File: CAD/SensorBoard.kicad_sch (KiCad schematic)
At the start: 82 parts, among them J1 USB C 2.0, J2 SWD Connector, J3 UART Connector, J4 DAC Connector, M1 M1, M2 M2, M3 M3, M4 M4, SW1 SW_1, SW2 SW_2, SW3 SW_3, SW4 SW_4, SW5 SW_BOOT, SW6 SW_RST, U1 STM32U073CCT6, U2 MIC5365, U3 USBLC6-2SC6, U4 BME680, U5 BMI323, U6 TC1047, X1 32MHz, X2 32kHz768

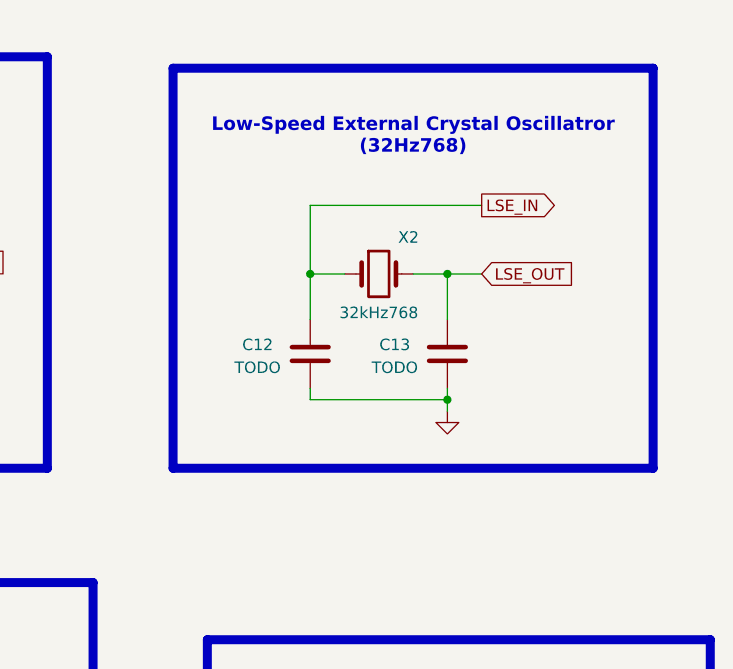
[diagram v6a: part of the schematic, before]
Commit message: Update oscillator footprint
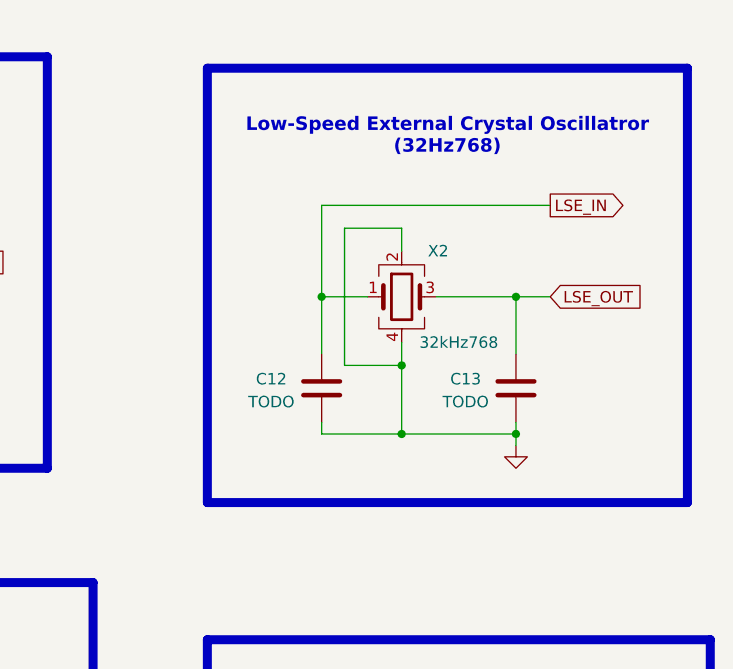
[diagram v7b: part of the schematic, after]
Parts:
- removed X2: 32kHz768, Crystal:Crystal_SMD_2012-2Pin_2.0x1.2mm, symbol Device:Crystal
- added X2: 32kHz768, SensorBoard:Crystal_SMD_2016-4Pin_2.0x1.6mm, symbol Device:Crystal_GND24
- X1: footprint Crystal:Crystal_SMD_2016-4Pin_2.0x1.6mm -> SensorBoard:Crystal_SMD_2016-4Pin_2.0x1.6mm
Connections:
- net GND: now also X2.2, X2.4
- net LSE_IN: now also X2.1
- net LSE_OUT: now also X2.3

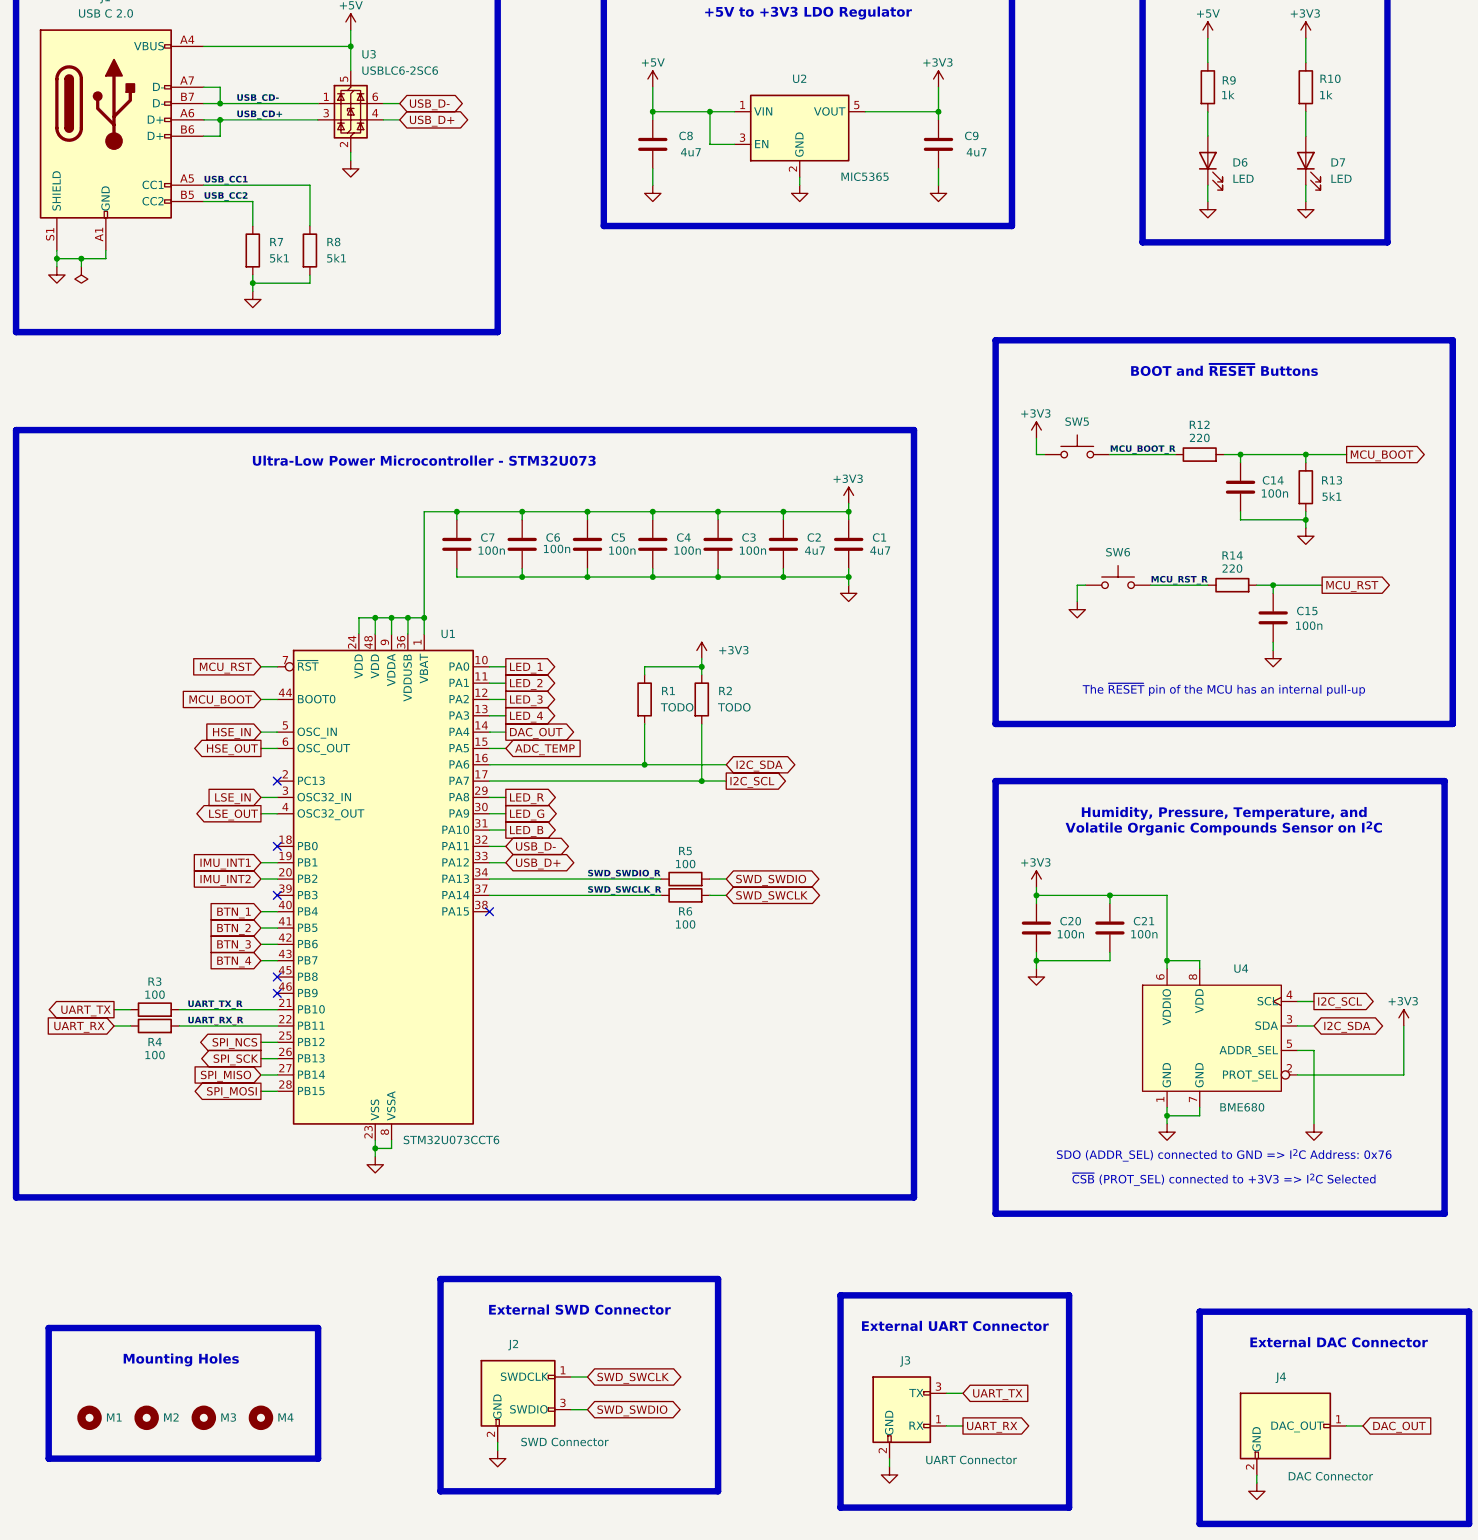
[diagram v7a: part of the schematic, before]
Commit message: Finish rough components placement
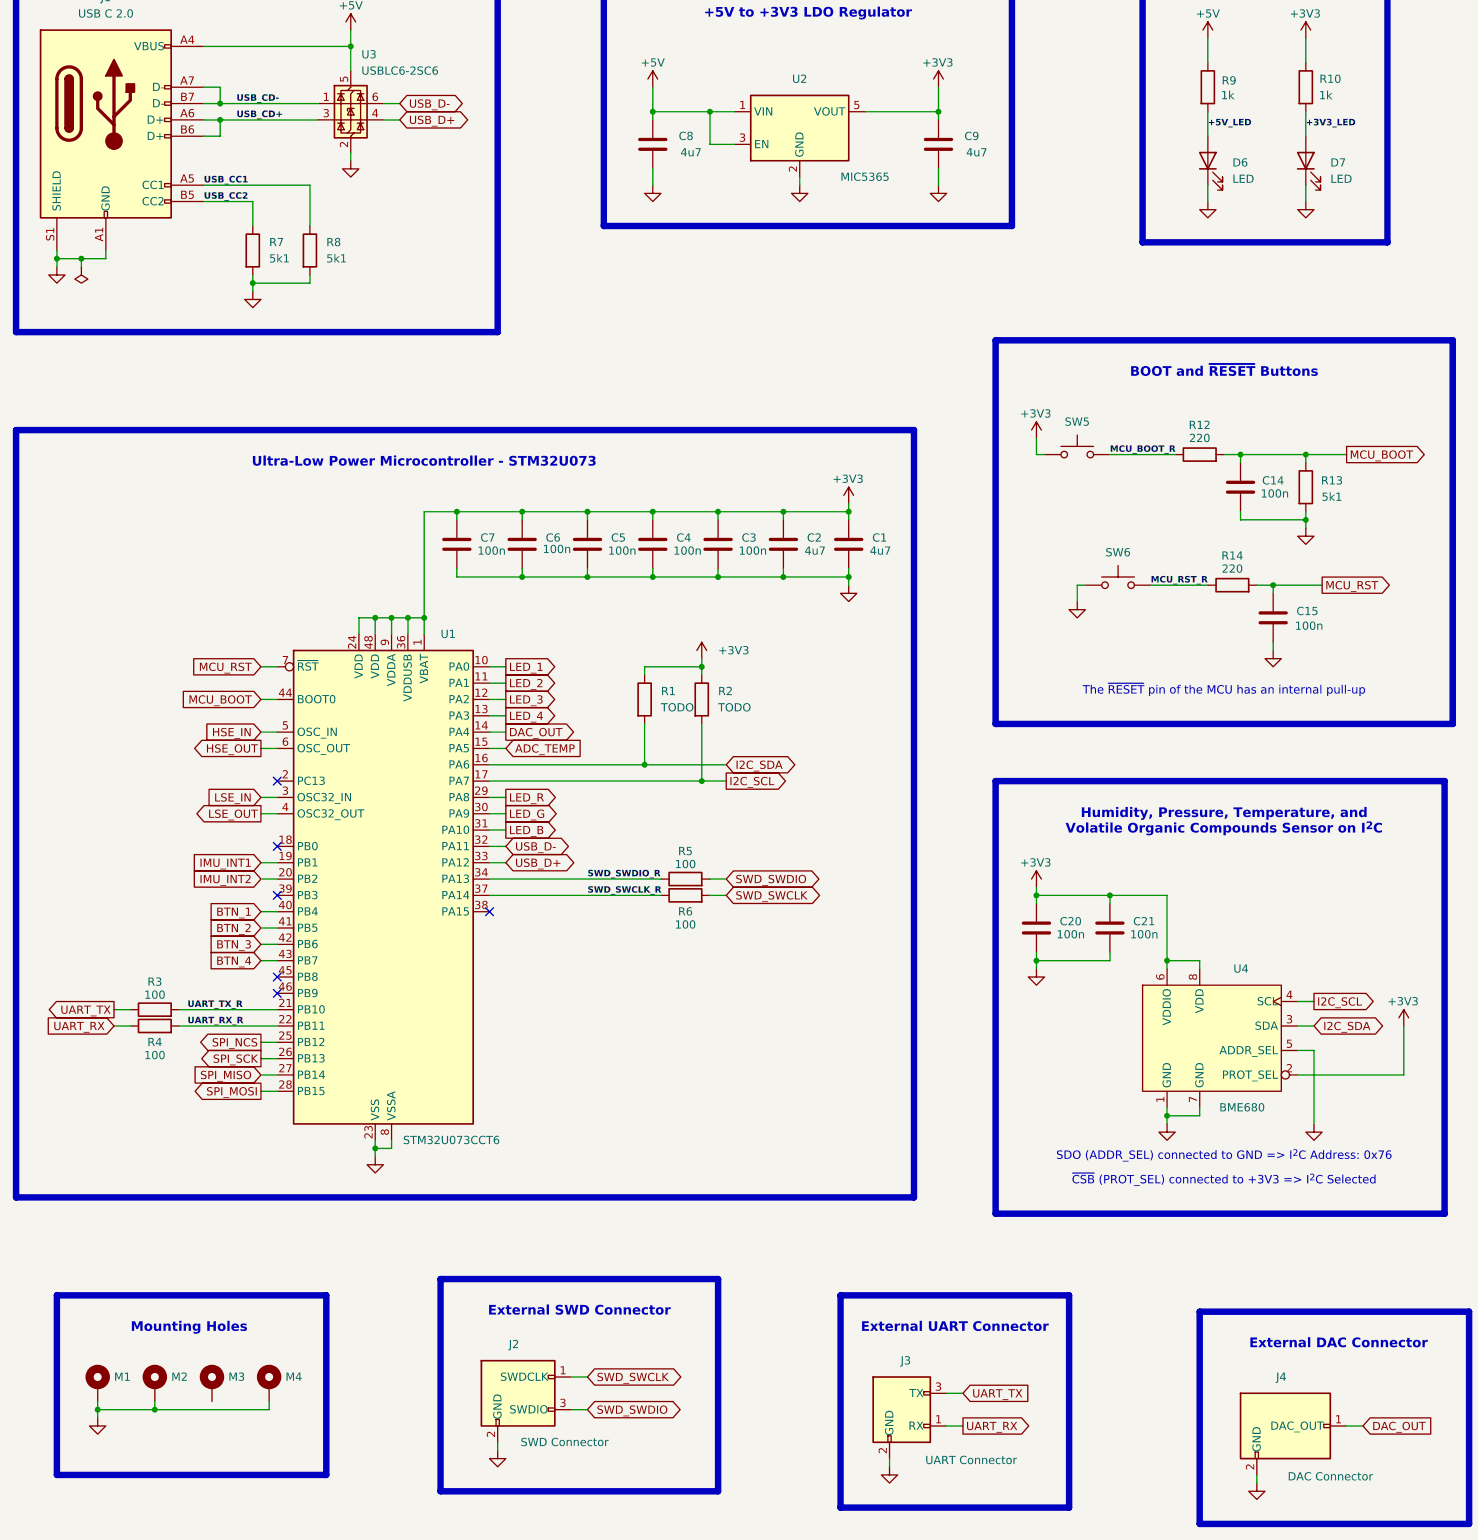
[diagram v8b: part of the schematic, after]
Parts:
- M1, M2, M3, M4: symbol Mechanical:MountingHole -> Mechanical:MountingHole_Pad
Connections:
- net GND: now also M1.1, M2.1, M4.1
- net +3V3_LED: now reaches D7.2 (A), R10.2
- net +5V_LED: now reaches D6.2 (A), R9.2
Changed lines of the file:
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@@
 	)
 	(junction
+		(at 45.72 256.54)
+		(diameter 0)
+		(color 0 0 0 0)
+	)
+	(junction
 		(at 182.88 176.53)
 		(diameter 0)
@@
 	)
 	(junction
+		(at 36.83 256.54)
+		(diameter 0)
+		(color 0 0 0 0)
+	)
+	(junction
 		(at 389.89 135.89)
 		(diameter 0)
@@
 	(wire
 		(pts
+			(xy 45.72 256.54) (xy 36.83 256.54)
+		)
+		(stroke
+			(width 0)
+			(type default)
+		)
+	)
+	(wire
+		(pts
 			(xy 297.18 135.89) (xy 307.34 135.89)
 		)
@@
 	(wire
 		(pts
+			(xy 36.83 255.27) (xy 36.83 256.54)
+		)
+		(stroke
+			(width 0)
+			(type default)
+		)
+	)
+	(wire
+		(pts
 			(xy 97.79 156.21) (xy 121.92 156.21)
 		)
@@
 	(wire
 		(pts
+			(xy 63.5 255.27) (xy 63.5 256.54)
+		)
+		(stroke
+			(width 0)
+			(type default)
+		)
+	)
+	(wire
+		(pts
 			(xy 130.81 140.97) (xy 130.81 142.24)
 		)
@@
 	(wire
 		(pts
+			(xy 45.72 255.27) (xy 45.72 256.54)
+		)
+		(stroke
+			(width 0)
+			(type default)
+		)
+	)
+	(wire
+		(pts
 			(xy 279.4 135.89) (xy 287.02 135.89)
 		)
@@
 	(wire
 		(pts
+			(xy 36.83 256.54) (xy 36.83 257.81)
+		)
+		(stroke
+			(width 0)
+			(type default)
+		)
+	)
+	(wire
+		(pts
 			(xy 351.79 128.27) (xy 358.14 128.27)
 		)
@@
 	(wire
 		(pts
+			(xy 63.5 256.54) (xy 45.72 256.54)
+		)
+		(stroke
+			(width 0)
+			(type default)
+		)
+	)
+	(wire
+		(pts
 			(xy 143.51 116.84) (xy 153.67 116.84)
 		)
@@
 	)
 	(rectangle
-		(start 29.21 243.84)
-		(end 71.12 264.16)
+		(start 30.48 238.76)
+		(end 72.39 266.7)
 		(stroke
 			(width 1)
@@
 	(text "Mounting Holes\n"
 		(exclude_from_sim no)
-		(at 49.784 248.92 0)
+		(at 51.054 243.84 0)
 		(effects
 			(font
@@
 		)
 	)
+	(label "+3V3_LED"
+		(at 224.79 57.15 0)
+		(fields_autoplaced yes)
+		(effects
+			(font
+				(size 1 1)
+				(thickness 0.254)
+				(bold yes)
+			)
+			(justify left bottom)
+		)
+	)
 	(label "SWD_SWDIO_R"
 		(at 113.03 173.99 0)
@@
 		)
 	)
+	(label "+5V_LED"
+		(at 209.55 57.15 0)
+		(fields_autoplaced yes)
+		(effects
+			(font
+				(size 1 1)
+				(thickness 0.254)
+				(bold yes)
+			)
+			(justify left bottom)
+		)
+	)
 	(label "UART_RX_R"
 		(at 50.8 196.85 0)
@@
 	)
 	(symbol
-		(lib_id "Mechanical:MountingHole")
-		(at 44.45 257.81 0)
+		(lib_id "Mechanical:MountingHole_Pad")
+		(at 45.72 252.73 0)
 		(unit 1)
 		(exclude_from_sim yes)
@@
 		(fields_autoplaced yes)
 		(property "Reference" "M2"
-			(at 46.99 257.8099 0)
+			(at 48.26 251.4599 0)
 			(effects
 				(font
@@
 		)
 		(property "Value" "M2"
-			(at 46.99 257.8099 0)
+			(at 48.26 252.7299 0)
 			(effects
 				(font
@@
 		)
 		(property "Footprint" "MountingHole:MountingHole_3.2mm_M3_Pad_Via"
-			(at 44.45 257.81 0)
+			(at 45.72 252.73 0)
 			(effects
 				(font
@@
 		)
 		(property "Datasheet" "~"
-			(at 44.45 257.81 0)
+			(at 45.72 252.73 0)
 			(effects
 				(font
@@
 			)
 		)
-		(property "Description" "Mounting Hole without connection"
-			(at 44.45 257.81 0)
+		(property "Description" "Mounting Hole with connection"
+			(at 45.72 252.73 0)
 			(effects
 				(font
@@
 			)
 		)
+		(pin "1"
+		)
 		(instances
 			(project "SensorBoard"
@@
 	)
 	(symbol
-		(lib_id "Mechanical:MountingHole")
-		(at 62.23 257.81 0)
+		(lib_id "Mechanical:MountingHole_Pad")
+		(at 63.5 252.73 0)
 		(unit 1)
 		(exclude_from_sim yes)
@@
 		(fields_autoplaced yes)
 		(property "Reference" "M4"
-			(at 64.77 257.8099 0)
+			(at 66.04 251.4599 0)
 			(effects
 				(font
@@
 		)
 		(property "Value" "M4"
-			(at 64.77 257.8099 0)
+			(at 66.04 252.7299 0)
 			(effects
 				(font
@@
 		)
 		(property "Footprint" "MountingHole:MountingHole_3.2mm_M3_Pad_Via"
-			(at 62.23 257.81 0)
+			(at 63.5 252.73 0)
 			(effects
 				(font
@@
 		)
 		(property "Datasheet" "~"
-			(at 62.23 257.81 0)
+			(at 63.5 252.73 0)
 			(effects
 				(font
@@
 			)
 		)
-		(property "Description" "Mounting Hole without connection"
-			(at 62.23 257.81 0)
+		(property "Description" "Mounting Hole with connection"
+			(at 63.5 252.73 0)
 			(effects
 				(font
@@
 			)
 		)
+		(pin "1"
+		)
 		(instances
 			(project "SensorBoard"
@@
 	)
 	(symbol
-		(lib_id "Mechanical:MountingHole")
-		(at 35.56 257.81 0)
+		(lib_id "Mechanical:MountingHole_Pad")
+		(at 36.83 252.73 0)
 		(unit 1)
 		(exclude_from_sim yes)
@@
 		(fields_autoplaced yes)
 		(property "Reference" "M1"
-			(at 38.1 257.8099 0)
+			(at 39.37 251.4599 0)
 			(effects
 				(font
@@
 		)
 		(property "Value" "M1"
-			(at 38.1 257.8099 0)
+			(at 39.37 252.7299 0)
 			(effects
 				(font
@@
 		)
 		(property "Footprint" "MountingHole:MountingHole_3.2mm_M3_Pad_Via"
-			(at 35.56 257.81 0)
+			(at 36.83 252.73 0)
 			(effects
 				(font
@@
 		)
 		(property "Datasheet" "~"
-			(at 35.56 257.81 0)
+			(at 36.83 252.73 0)
 			(effects
 				(font
@@
 			)
 		)
-		(property "Description" "Mounting Hole without connection"
-			(at 35.56 257.81 0)
+		(property "Description" "Mounting Hole with connection"
+			(at 36.83 252.73 0)
 			(effects
 				(font
@@
 			)
 		)
+		(pin "1"
+		)
 		(instances
 			(project ""
@@
 	)
 	(symbol
-		(lib_id "Mechanical:MountingHole")
-		(at 53.34 257.81 0)
+		(lib_id "Mechanical:MountingHole_Pad")
+		(at 54.61 252.73 0)
 		(unit 1)
 		(exclude_from_sim yes)
@@
 		(fields_autoplaced yes)
 		(property "Reference" "M3"
-			(at 55.88 257.8099 0)
+			(at 57.15 251.4599 0)
 			(effects
 				(font
@@
 		)
 		(property "Value" "M3"
-			(at 55.88 257.8099 0)
+			(at 57.15 252.7299 0)
 			(effects
 				(font
@@
 		)
 		(property "Footprint" "MountingHole:MountingHole_3.2mm_M3_Pad_Via"
-			(at 53.34 257.81 0)
+			(at 54.61 252.73 0)
 			(effects
 				(font
@@
 		)
 		(property "Datasheet" "~"
-			(at 53.34 257.81 0)
+			(at 54.61 252.73 0)
 			(effects
 				(font
@@
 			)
 		)
-		(property "Description" "Mounting Hole without connection"
-			(at 53.34 257.81 0)
+		(property "Description" "Mounting Hole with connection"
+			(at 54.61 252.73 0)
 			(effects
 				(font
@@
 			)
 		)
+		(pin "1"
+		)
 		(instances
 			(project "SensorBoard"
@@
 					(unit 1)
 				)
+			)
+		)
+	)
+	(symbol
+		(lib_id "power:GND")
+		(at 36.83 257.81 0)
+		(unit 1)
+		(exclude_from_sim no)
+		(in_bom yes)
+		(on_board yes)
+		(dnp no)
+		(fields_autoplaced yes)
+		(property "Reference" "#PWR026"
+			(at 36.83 264.16 0)
+			(effects
+				(font
+					(face "IBM Plex Sans")
+					(size 1.27 1.27)
+				)
+				(hide yes)
+			)
+		)
+		(property "Value" "GND"
+			(at 36.83 262.89 0)
+			(effects
+				(font
+					(face "IBM Plex Sans")
+					(size 1.27 1.27)
+				)
+				(hide yes)
+			)
+		)
+		(property "Footprint" ""
+			(at 36.83 257.81 0)
+			(effects
+				(font
+					(face "IBM Plex Sans")
+					(size 1.27 1.27)
+				)
+				(hide yes)
+			)
+		)
+		(property "Datasheet" ""
+			(at 36.83 257.81 0)
+			(effects
+				(font
+					(face "IBM Plex Sans")
+					(size 1.27 1.27)
+				)
+				(hide yes)
+			)
+		)
+		(property "Description" "Power symbol creates a global label with name \"GND\" , ground"
+			(at 36.83 257.81 0)
+			(effects
+				(font
+					(face "IBM Plex Sans")
+					(size 1.27 1.27)
+				)
+				(hide yes)
+			)
+		)
+		(pin "1"
+		)
+		(instances
+			(project "SensorBoard"
+				(path "/56f2708f-e6aa-4b97-8a34-e15d8ff6695d"
+					(reference "#PWR026")
+					(unit 1)
+				)
